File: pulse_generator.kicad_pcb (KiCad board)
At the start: 4 copper layers, 82.6 x 53 mm, 31 parts, among them J1 Power, J2 Digital/PWM, J3 Analog, J4 Digital/PWM, J5 Conn_Coaxial, J6 Conn_Coaxial, SW1 SW_Push, U1 LM311, U2 74LS279

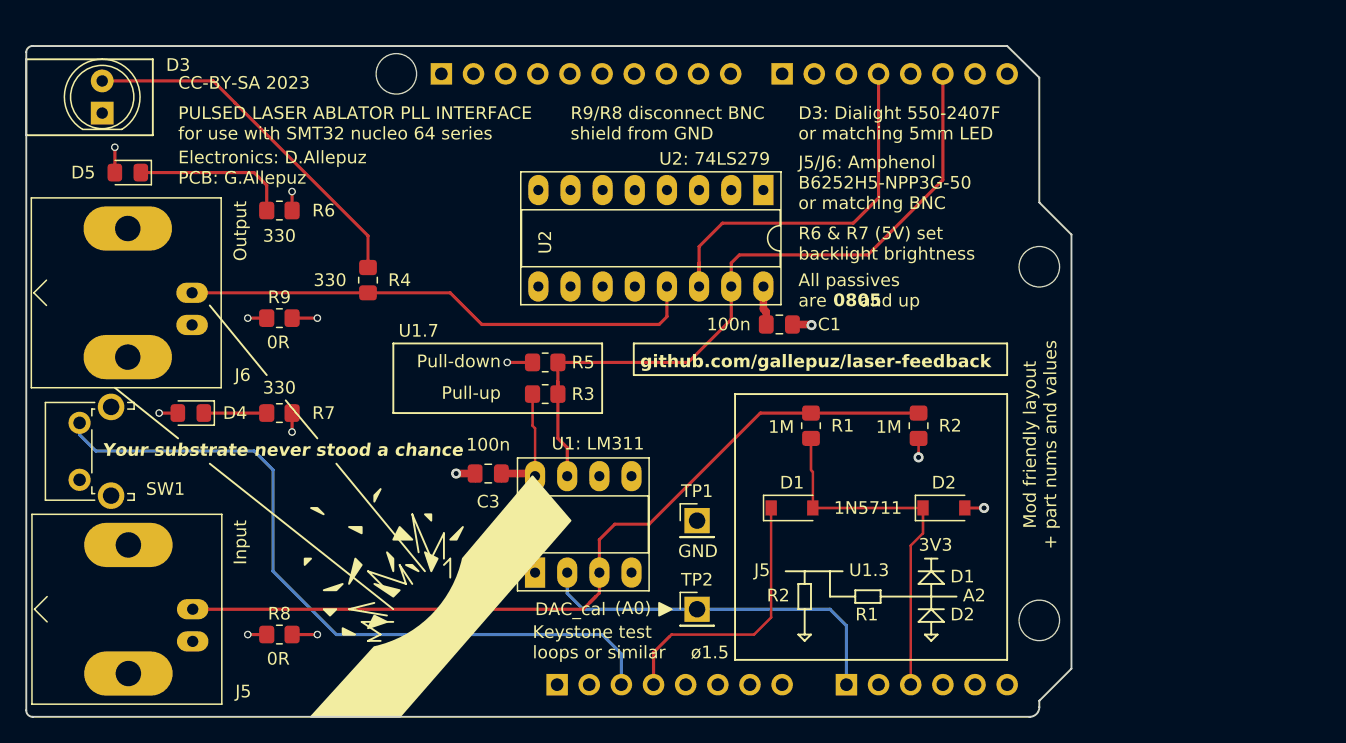
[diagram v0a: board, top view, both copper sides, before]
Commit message: rearrange diode clamp section
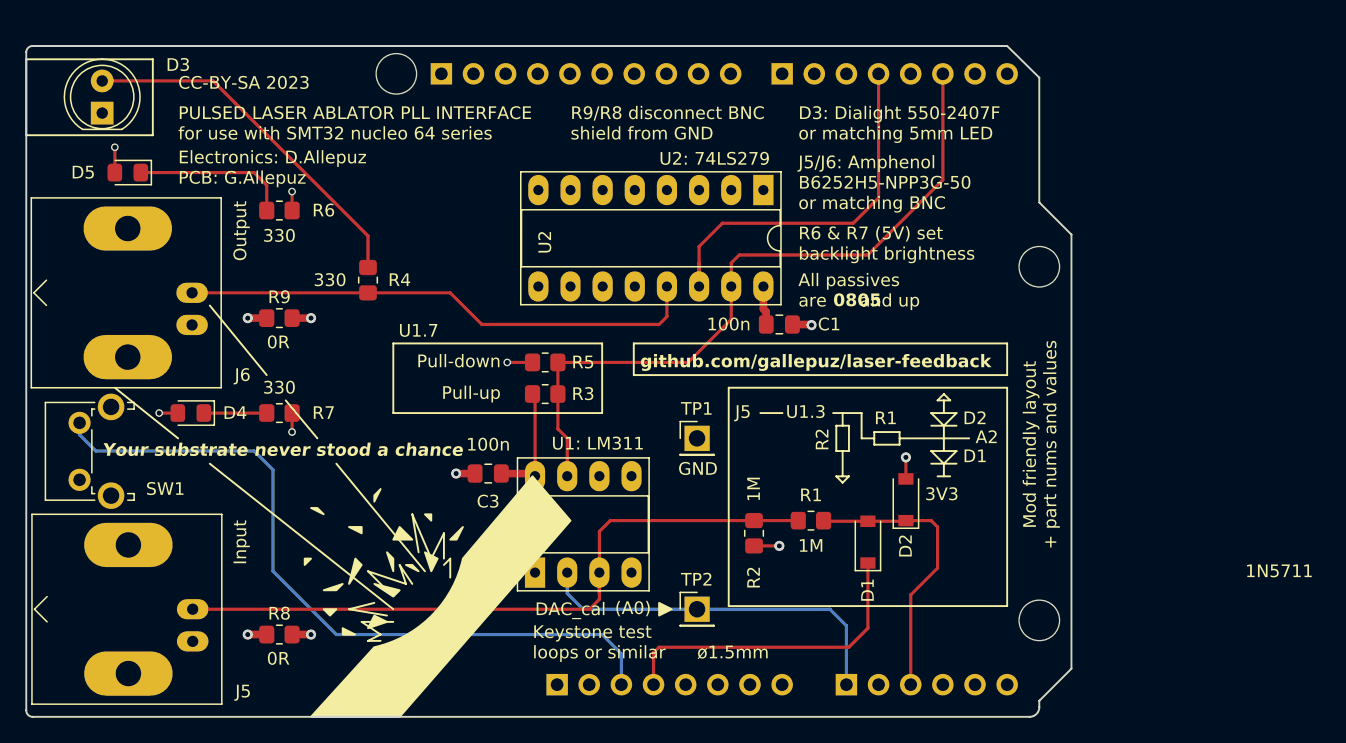
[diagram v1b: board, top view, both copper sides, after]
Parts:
- moved R2 15.5 mm to (143.5, 85.5)
- moved R1 7.50 mm to (148.0, 84.5), turned to 0 degrees
- moved D1 6.58 mm to (152.5, 86.2), turned to 90 degrees
- moved TP1 6.50 mm to (139.0, 78.0)
- moved D2 3.07 mm to (155.5, 82.8), turned to 90 degrees
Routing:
- net Net-(J5-In): track 67.0 -> 55.5 mm
- net /A2: track 28.6 -> 22.6 mm
- net +3V3: track 21.6 -> 25.4 mm
- net /2: track 59.1 -> 58.1 mm
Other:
- board text added: "ø1.5mm"
- board text removed: "ø1.5"

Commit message: Please enter the commit message for your changes. Lines starting
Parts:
- J1, J2, J3, J4: moved to F.Cu
- moved C3 0.93 mm to (122.0, 80.0)
- moved U1 0.64 mm to (126.0, 88.0)
- moved C1 0.50 mm to (145.0, 69.0)
- moved U2 0.45 mm to (144.0, 58.0)
- turned J4 to 90 degrees
- turned J2 to 90 degrees
- turned J1 to 90 degrees
- turned J3 to 90 degrees
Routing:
- net /4: track 30.6 -> 28.4 mm
- net Net-(J5-In): track 55.5 -> 54.0 mm
- net /2: track 58.1 -> 56.8 mm
- net /A0: track 29.4 -> 30.4 mm
- net +5V: track 17.8 -> 18.4 mm
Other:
- board text added: "1N58"
- board text added: "Notes about this board:"
- board text added: "WayWayWay"
- board text removed: "1N5711"
